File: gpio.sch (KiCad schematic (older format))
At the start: 5 parts, among them J1 CONN_02X20, J2 CONN_02X20, U1 LFE5U-85F-6BG381C

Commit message: schematics: PN update
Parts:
- U1: Mouser_URL www.mouser.com -> (none)
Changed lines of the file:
@@
 F 3 "http://www.latticesemi.com/~/media/LatticeSemi/Documents/DataSheets/ECP5/FPGA-DS-02012.pdf" H 3850 5700 60  0001 C CNN
 F 4 "LFE5U-85F-6BG381C" H 4900 4750 60  0001 C CNN "MPN"
-F 5 "www.mouser.com" H 4900 4750 60  0001 C CNN "Mouser_URL"
-F 6 "842-LFE5U85F6BG381C" H 4900 4750 60  0001 C CNN "Mouser"
+F 5 "842-LFE5U85F6BG381C" H 4900 4750 60  0001 C CNN "Mouser"
 	6    4900 4750
 	1    0    0    -1
@@
 F 3 "http://www.latticesemi.com/~/media/LatticeSemi/Documents/DataSheets/ECP5/FPGA-DS-02012.pdf" H 3900 3450 60  0001 C CNN
 F 4 "LFE5U-85F-6BG381C" H 4950 2500 60  0001 C CNN "MPN"
-F 5 "www.mouser.com" H 4950 2500 60  0001 C CNN "Mouser_URL"
-F 6 "842-LFE5U85F6BG381C" H 4950 2500 60  0001 C CNN "Mouser"
+F 5 "842-LFE5U85F6BG381C" H 4950 2500 60  0001 C CNN "Mouser"
 	1    4950 2500
 	1    0    0    -1

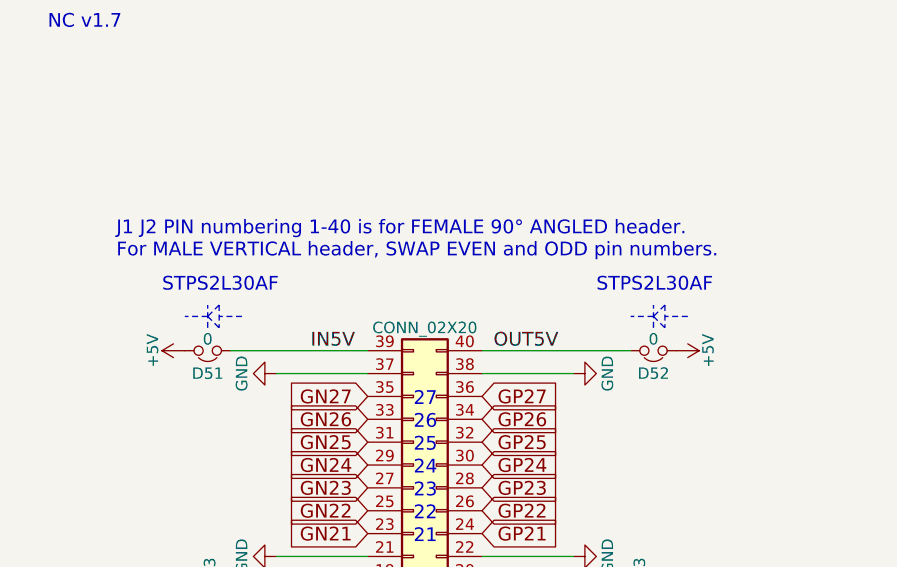
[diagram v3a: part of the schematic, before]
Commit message: schematics: updating PN currently available from mouser
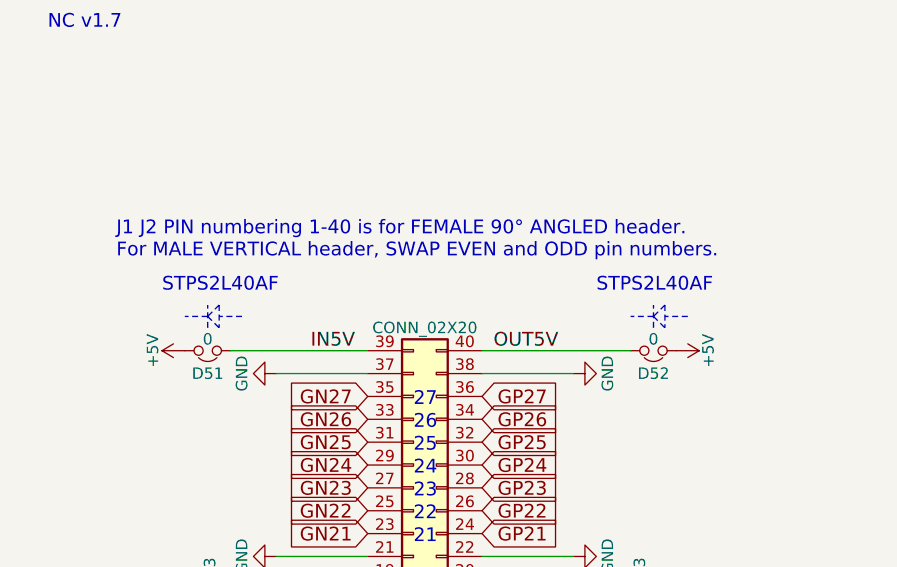
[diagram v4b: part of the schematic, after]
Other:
- note added: "STPS2L40AF"
- note removed: "STPS2L30AF"
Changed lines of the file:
@@
 	7450 3500 7350 3500
 Text Notes 7250 3400 0    60   ~ 0
-STPS2L30AF
+STPS2L40AF
 Wire Notes Line
 	9550 3500 9450 3500
@@
 	9400 3500 9300 3500
 Text Notes 9150 3400 0    60   ~ 0
-STPS2L30AF
+STPS2L40AF
 NoConn ~ 4200 3000
 NoConn ~ 4200 3100

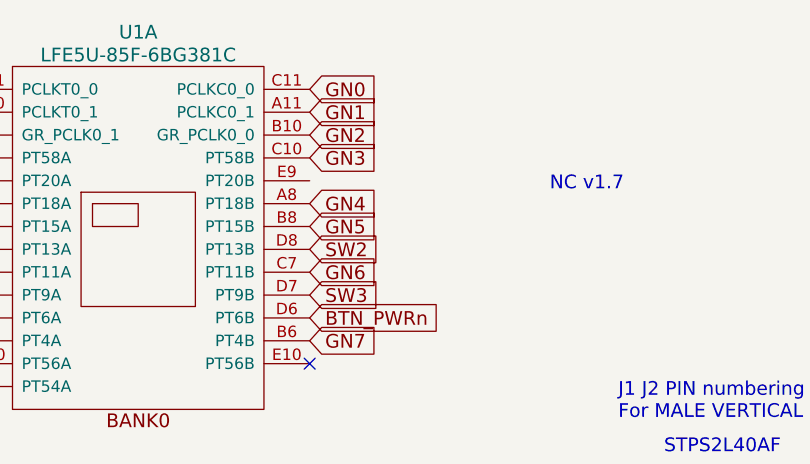
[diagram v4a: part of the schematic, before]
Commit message: schematics: wifi_gpio25
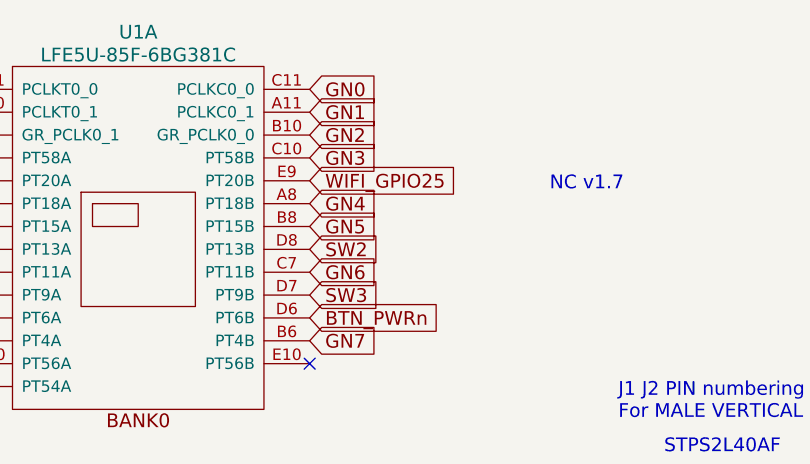
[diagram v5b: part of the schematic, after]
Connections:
- net WIFI_GPIO25: now reaches U1.E9 (PT20B)
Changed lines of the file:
@@
 Text Notes 7050 3250 0    60   ~ 0
 J1 J2 PIN numbering 1-40 is for FEMALE 90° ANGLED header.\nFor MALE VERTICAL header, SWAP EVEN and ODD pin numbers.
+Text GLabel 5700 2200 2    60   Input ~ 0
+WIFI_GPIO25
 $EndSCHEMATC

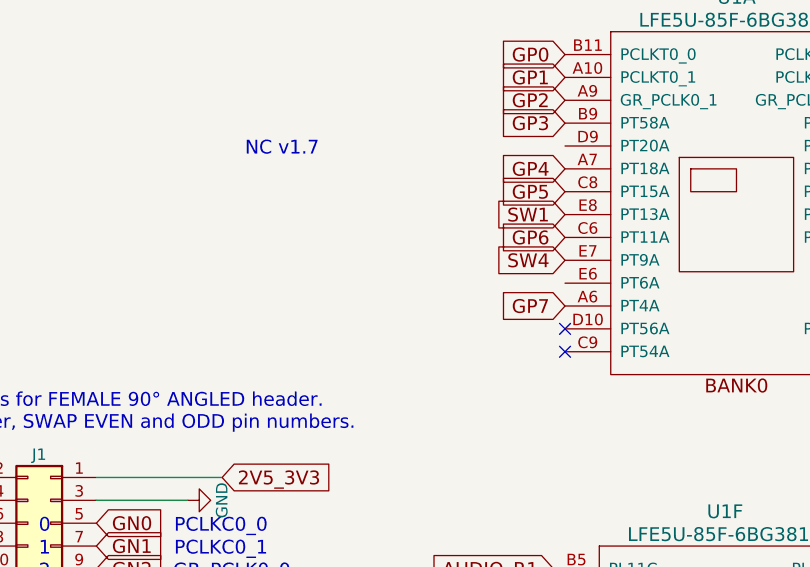
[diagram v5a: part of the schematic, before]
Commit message: schematics: wifi_gpio35 directly to FPGA
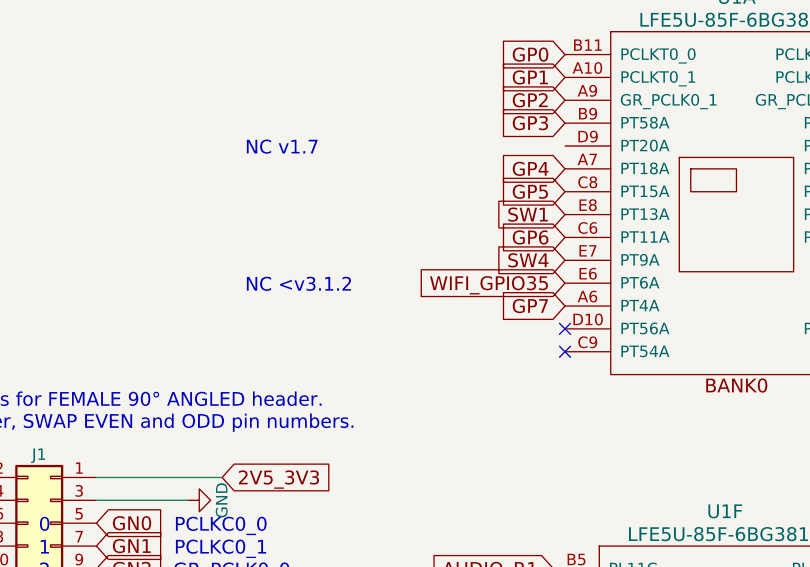
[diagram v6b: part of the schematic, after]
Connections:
- net WIFI_GPIO35: now reaches U1.E6 (PT6A)
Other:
- note added: "NC <v3.1.2"
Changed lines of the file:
@@
 Title "ULX3S"
 Date ""
-Rev "1.0.1"
+Rev "1.0.2"
 Comp "EMARD"
 Comment1 "GPIO 2.54 mm connectors"
@@
 Text GLabel 5700 2200 2    60   Input ~ 0
 WIFI_GPIO25
+Text GLabel 4200 2800 0    60   Input ~ 0
+WIFI_GPIO35
+Text Notes 2800 2850 0    60   ~ 0
+NC <v3.1.2
 $EndSCHEMATC

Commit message: schematics: switch to serdes symbol
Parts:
- U1: symbol lfe5bg381:LFE5U-85F-6BG381C -> lfe5bg381:LFE5UM-85F-6BG381C
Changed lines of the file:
@@
 AUDIO_V0
 $Comp
-L lfe5bg381:LFE5U-85F-6BG381C U1
+L lfe5bg381:LFE5UM-85F-6BG381C U1
 U 6 1 5A0783C9
 P 4900 4750
@@
 $EndComp
 $Comp
-L lfe5bg381:LFE5U-85F-6BG381C U1
+L lfe5bg381:LFE5UM-85F-6BG381C U1
 U 1 1 5A0737C6
 P 4950 2500

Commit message: schematics: digikey PN for 85F
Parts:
- U1: Mouser 842-LFE5U85F6BG381C -> (none)
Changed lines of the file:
@@
 F 3 "http://www.latticesemi.com/~/media/LatticeSemi/Documents/DataSheets/ECP5/FPGA-DS-02012.pdf" H 3850 5700 60  0001 C CNN
 F 4 "LFE5U-85F-6BG381C" H 4900 4750 60  0001 C CNN "MPN"
-F 5 "842-LFE5U85F6BG381C" H 4900 4750 60  0001 C CNN "Mouser"
 	6    4900 4750
 	1    0    0    -1
@@
 F 3 "http://www.latticesemi.com/~/media/LatticeSemi/Documents/DataSheets/ECP5/FPGA-DS-02012.pdf" H 3900 3450 60  0001 C CNN
 F 4 "LFE5U-85F-6BG381C" H 4950 2500 60  0001 C CNN "MPN"
-F 5 "842-LFE5U85F6BG381C" H 4950 2500 60  0001 C CNN "Mouser"
 	1    4950 2500
 	1    0    0    -1
